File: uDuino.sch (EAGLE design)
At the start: 20 parts, among them IC1 LM7805, IC2 ATMEGA328, J1 POWER_JACK", Q1 16MHZ

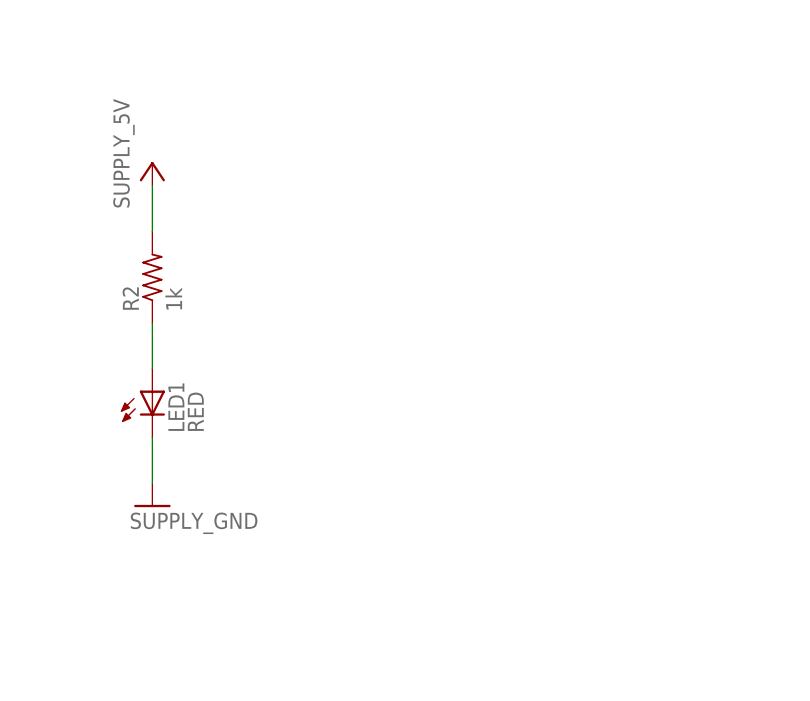
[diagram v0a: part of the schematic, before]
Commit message: Added LED at D13
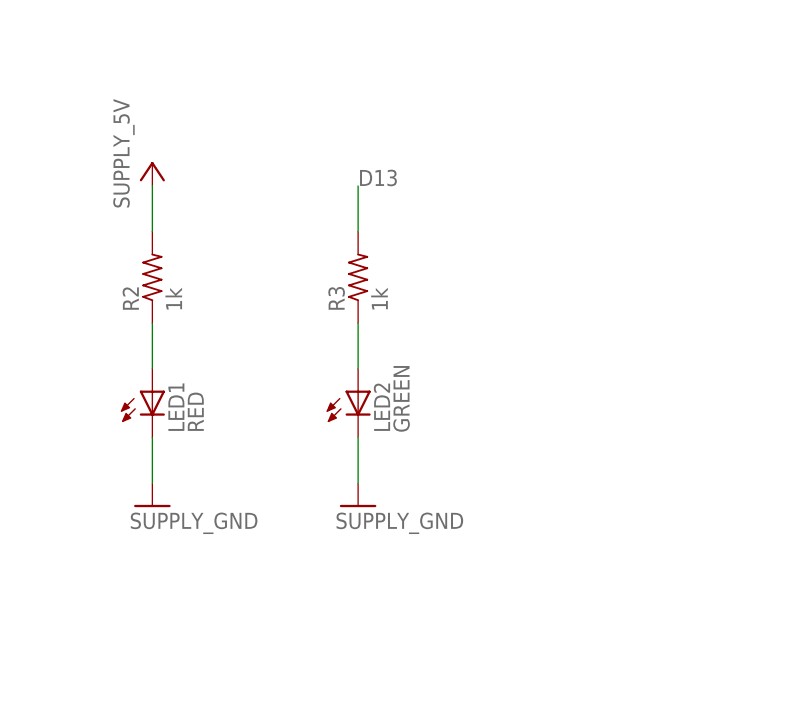
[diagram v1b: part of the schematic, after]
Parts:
- added LED2: GREEN, adafruit:LED5MM
- added R3: 1k, adafruit:R-US_0204/7
- LED1: device RBBB:LED3MM -> adafruit:LED5MM
- R1, R2: device RBBB:RESISTOR1/6WATT -> adafruit:R-US_0204/7
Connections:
- new net N$4: LED2.A, R3.1
- net D13: now also R3.2
- net GND: now also LED2.C
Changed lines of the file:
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@@
 <part name="JP4" library="RBBB" deviceset="1X06_HEADER" device="&quot;" value="1X06_HEADER&quot;"/>
 <part name="S1" library="RBBB" deviceset="MOMENTARY_SWITCH" device="&quot;"/>
-<part name="R1" library="RBBB" deviceset="RESISTOR" device="1/6WATT" value="10k"/>
+<part name="R1" library="adafruit" deviceset="R-US_" device="0204/7" value="10k"/>
 <part name="C6" library="RBBB" deviceset="UNPOLARIZED_CAP" device="&quot;" value="0.1uF"/>
 <part name="P+3" library="RBBB" deviceset="SUPPLY_5V" device=""/>
 <part name="GND3" library="RBBB" deviceset="SUPPLY_GND" device=""/>
-<part name="LED1" library="RBBB" deviceset="LED" device="3MM" value="RED"/>
-<part name="R2" library="RBBB" deviceset="RESISTOR" device="1/6WATT" value="1k"/>
+<part name="LED1" library="adafruit" deviceset="LED" device="5MM" value="RED"/>
+<part name="R2" library="adafruit" deviceset="R-US_" device="0204/7" value="1k"/>
+<part name="R3" library="adafruit" deviceset="R-US_" device="0204/7" value="1k"/>
+<part name="LED2" library="adafruit" deviceset="LED" device="5MM" value="GREEN"/>
+<part name="GND4" library="RBBB" deviceset="SUPPLY_GND" device=""/>
 </parts>
 <sheets>
@@
 <instance part="LED1" gate="G$1" x="101.6" y="53.34"/>
 <instance part="R2" gate="G$1" x="101.6" y="66.04" rot="R90"/>
+<instance part="R3" gate="G$1" x="124.46" y="66.04" rot="R90"/>
+<instance part="LED2" gate="G$1" x="124.46" y="53.34"/>
+<instance part="GND4" gate="1" x="124.46" y="40.64"/>
 </instances>
 <busses>
@@
 <wire x1="101.6" y1="48.26" x2="101.6" y2="43.18" width="0.1524" layer="91"/>
 </segment>
+<segment>
+<pinref part="LED2" gate="G$1" pin="C"/>
+<pinref part="GND4" gate="1" pin="GND"/>
+<wire x1="124.46" y1="48.26" x2="124.46" y2="43.18" width="0.1524" layer="91"/>
+</segment>
 </net>
 <net name="N$2" class="0">
@@
 <wire x1="193.04" y1="104.14" x2="177.8" y2="104.14" width="0.1524" layer="91"/>
 <label x="177.8" y="104.14" size="1.778" layer="95"/>
+</segment>
+<segment>
+<pinref part="R3" gate="G$1" pin="2"/>
+<wire x1="124.46" y1="71.12" x2="124.46" y2="76.2" width="0.1524" layer="91"/>
+<label x="124.46" y="76.2" size="1.778" layer="95"/>
 </segment>
 </net>
@@
 </segment>
 </net>
+<net name="N$4" class="0">
+<segment>
+<pinref part="R3" gate="G$1" pin="1"/>
+<pinref part="LED2" gate="G$1" pin="A"/>
+<wire x1="124.46" y1="60.96" x2="124.46" y2="55.88" width="0.1524" layer="91"/>
+</segment>
+</net>

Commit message: changed frame
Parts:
- added FRAME1: FRAME-LETTERNO_PACKAGE, SparkFun-Aesthetics:FRAME-LETTERNO_PACKAGE
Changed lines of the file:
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@@
 <?xml version="1.0" encoding="utf-8"?>
 <!DOCTYPE eagle SYSTEM "eagle.dtd">
-<eagle version="8.0.1">
+<eagle version="8.2.1">
 <drawing>
 <settings>
@@
 <layer number="112" name="tSilk" color="7" fill="1" visible="yes" active="yes"/>
 <layer number="113" name="Paste_Add" color="7" fill="1" visible="yes" active="yes"/>
+<layer number="114" name="Badge_Outline" color="7" fill="1" visible="no" active="yes"/>
+<layer number="115" name="ReferenceISLANDS" color="7" fill="1" visible="no" active="yes"/>
 <layer number="116" name="Patch_BOT" color="7" fill="1" visible="yes" active="yes"/>
 <layer number="118" name="Rect_Pads" color="7" fill="1" visible="no" active="no"/>
@@
 </classes>
 <parts>
-<part name="FRAME1" library="RBBB" deviceset="FRAME_A_L" device="" value="FRAME"/>
 <part name="IC1" library="RBBB" deviceset="REGULATOR" device="" value="LM7805"/>
 <part name="C1" library="RBBB" deviceset="ELECTROLYTIC_CAP" device="2.54MM" value="10uF"/>
@@
 <part name="LED2" library="adafruit" deviceset="LED" device="5MM" value="GREEN"/>
 <part name="GND4" library="RBBB" deviceset="SUPPLY_GND" device=""/>
+<part name="FRAME1" library="SparkFun-Aesthetics" deviceset="FRAME-LETTER" device="NO_PACKAGE">
+<attribute name="DESIGNER" value="Ajay Meena"/>
+</part>
 </parts>
 <sheets>
@@
 </plain>
 <instances>
-<instance part="FRAME1" gate="G$1" x="-55.88" y="-58.42"/>
-<instance part="FRAME1" gate="G$2" x="116.84" y="-58.42"/>
 <instance part="IC1" gate="1" x="20.32" y="-2.54"/>
 <instance part="C1" gate="G$1" x="38.1" y="-10.16"/>
@@
 <instance part="LED2" gate="G$1" x="124.46" y="53.34"/>
 <instance part="GND4" gate="1" x="124.46" y="40.64"/>
+<instance part="FRAME1" gate="G$1" x="-35.56" y="-38.1" smashed="yes">
+<attribute name="DESIGNER" x="132.08" y="-27.94" size="2.7432" layer="94" font="vector"/>
+<attribute name="VERSION" x="200.66" y="-30.48" size="2.7432" layer="94" font="vector"/>
+</instance>
+<instance part="FRAME1" gate="V" x="111.76" y="-38.1" smashed="yes">
+<attribute name="LAST_DATE_TIME" x="124.46" y="-36.83" size="2.54" layer="94" font="vector"/>
+<attribute name="SHEET" x="198.12" y="-36.83" size="2.54" layer="94" font="vector"/>
+<attribute name="DRAWING_NAME" x="127.254" y="-20.32" size="2.7432" layer="94" font="vector"/>
+</instance>
 </instances>
 <busses>
